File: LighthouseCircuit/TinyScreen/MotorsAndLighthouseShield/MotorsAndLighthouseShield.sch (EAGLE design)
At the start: 29 parts

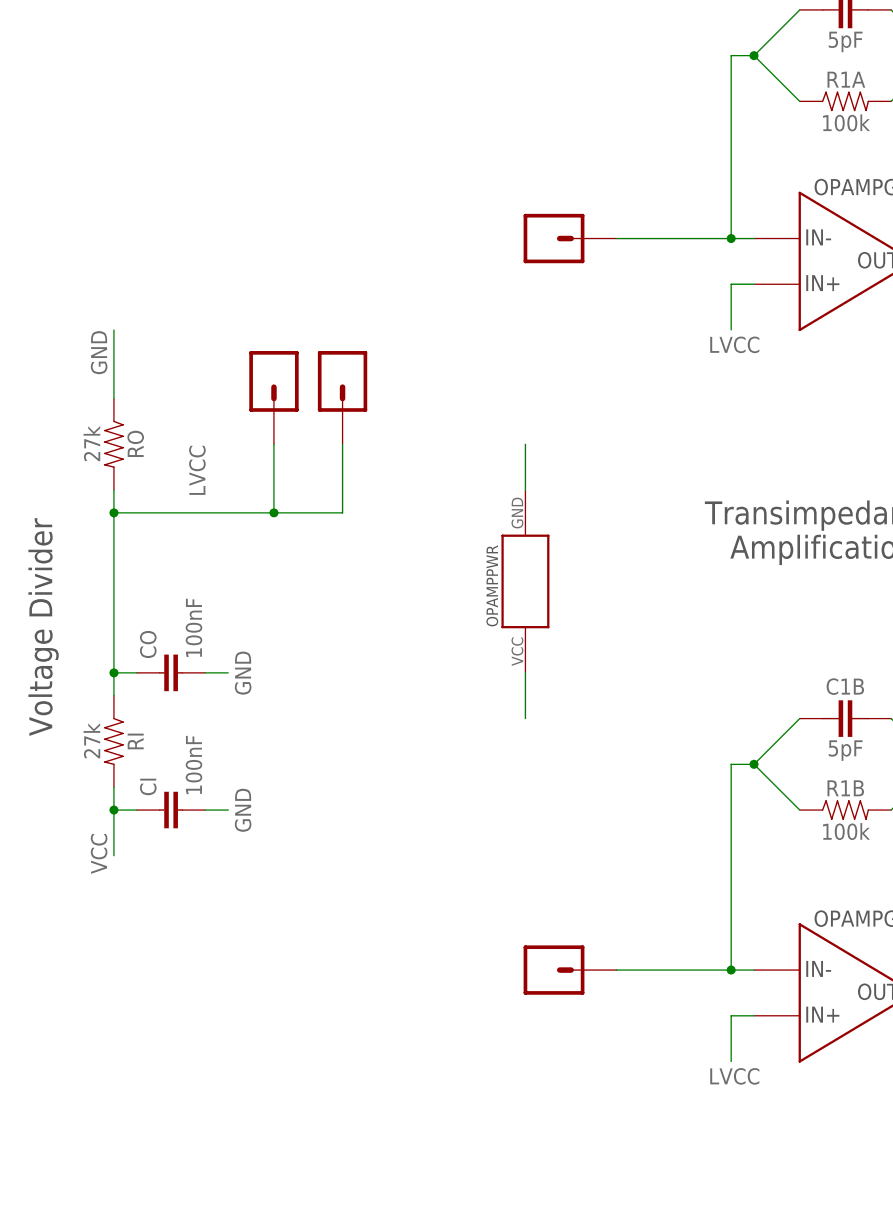
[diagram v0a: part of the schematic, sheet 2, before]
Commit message: Significantly stabilized the position calculation and the new driving model with independent PIDs for each wheel.
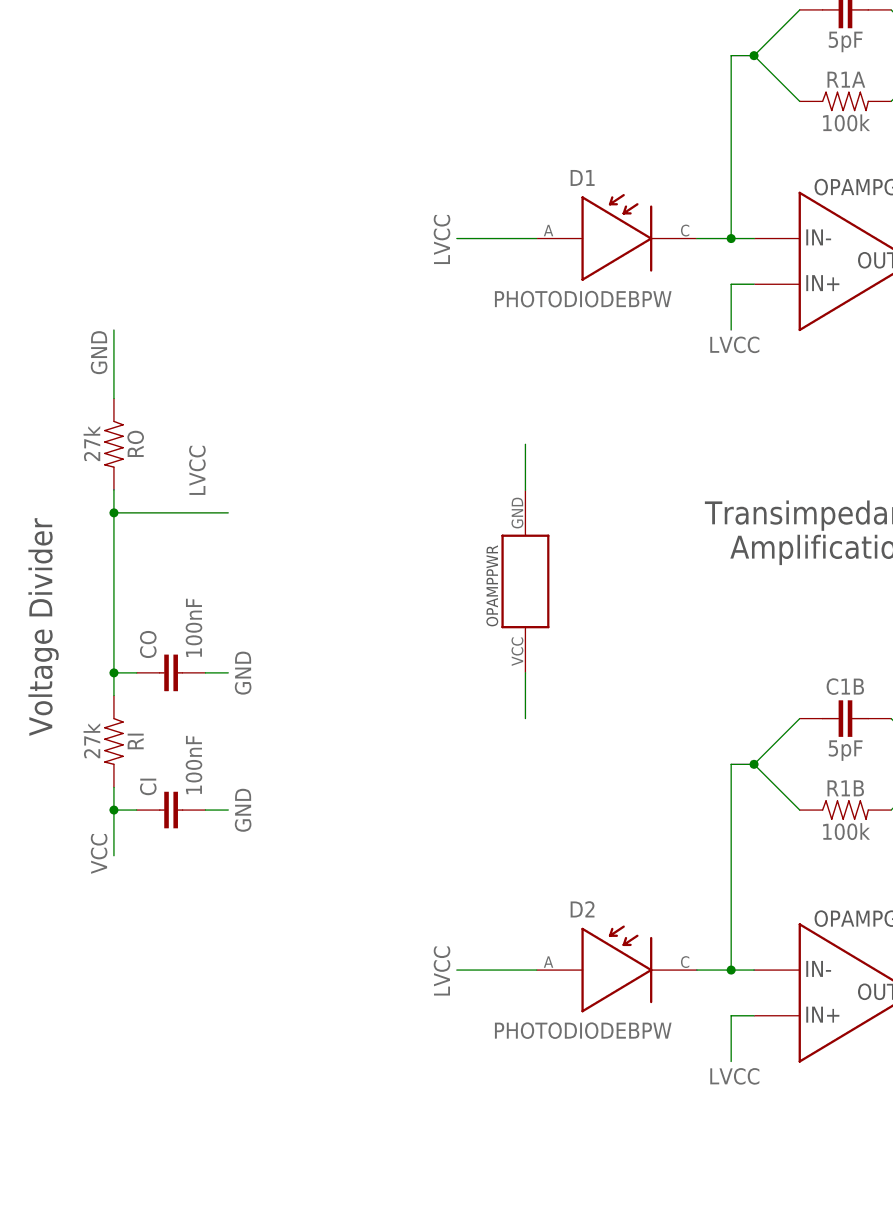
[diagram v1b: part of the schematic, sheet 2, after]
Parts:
- removed DIA, DIB, DOA, DOB: SINGLE-THROUGH-HOLE, ZippyComponentLibrary:SINGLE-THROUGH-HOLE
- added D1, D2: PHOTODIODEBPW, ZippyComponentLibrary:PHOTODIODEBPW
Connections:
- net D1IN1: now also D2.CATHODE; no longer DIB.1
- net D2IN1: now also D1.CATHODE; no longer DIA.1
- net IO6: now also MD.AIN1; no longer MD.BIN2
- net IO7: now also MD.AIN2; no longer MD.BIN1
- net IO8: now also MD.BIN1; no longer MD.AIN2
- net IO9: now also MD.BIN2; no longer MD.AIN1
- net LVCC: now also D1.ANODE, D2.ANODE; no longer DOA.1, DOB.1
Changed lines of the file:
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@@
 <part name="AO2" library="ZippyComponentLibrary" deviceset="SINGLE-THROUGH-HOLE" device=""/>
 <part name="HCM" library="ZippyComponentLibrary" deviceset="HIROSE-DF12-32DS" device="MALE" value="HIROSE-DF12-32DSMALE"/>
-<part name="DOA" library="ZippyComponentLibrary" deviceset="SINGLE-THROUGH-HOLE" device=""/>
-<part name="DIA" library="ZippyComponentLibrary" deviceset="SINGLE-THROUGH-HOLE" device=""/>
-<part name="DIB" library="ZippyComponentLibrary" deviceset="SINGLE-THROUGH-HOLE" device=""/>
-<part name="DOB" library="ZippyComponentLibrary" deviceset="SINGLE-THROUGH-HOLE" device=""/>
 <part name="VCO" library="ZippyComponentLibrary" deviceset="CAPACITOR" device="" value="0.1uF"/>
 <part name="VMO" library="ZippyComponentLibrary" deviceset="CAPACITOR" device="" value="0.1uF"/>
+<part name="D1" library="ZippyComponentLibrary" deviceset="PHOTODIODE" device="BPW"/>
+<part name="D2" library="ZippyComponentLibrary" deviceset="PHOTODIODE" device="BPW"/>
 </parts>
 <sheets>
@@
 </segment>
 <segment>
+<pinref part="MD" gate="A" pin="BIN2"/>
+<wire x1="208.28" y1="106.68" x2="200.66" y2="106.68" width="0.1524" layer="91"/>
+<label x="200.914" y="106.934" size="1.778" layer="95"/>
+</segment>
+</net>
+<net name="IO8" class="0">
+<segment>
+<pinref part="HCM" gate="G$1" pin="25"/>
+<wire x1="246.38" y1="25.4" x2="233.68" y2="25.4" width="0.1524" layer="91"/>
+<label x="233.426" y="25.654" size="1.778" layer="95"/>
+</segment>
+<segment>
+<pinref part="MD" gate="A" pin="BIN1"/>
+<wire x1="208.28" y1="109.22" x2="200.66" y2="109.22" width="0.1524" layer="91"/>
+<label x="200.914" y="109.474" size="1.778" layer="95"/>
+</segment>
+</net>
+<net name="IO3" class="0">
+<segment>
+<pinref part="HCM" gate="G$1" pin="30"/>
+<wire x1="269.24" y1="20.32" x2="279.4" y2="20.32" width="0.1524" layer="91"/>
+<label x="276.86" y="20.574" size="1.778" layer="95"/>
+</segment>
+</net>
+<net name="IO4" class="0">
+<segment>
+<pinref part="HCM" gate="G$1" pin="32"/>
+<wire x1="269.24" y1="17.78" x2="279.4" y2="17.78" width="0.1524" layer="91"/>
+<label x="276.86" y="18.034" size="1.778" layer="95"/>
+</segment>
+</net>
+<net name="IO6" class="0">
+<segment>
+<pinref part="HCM" gate="G$1" pin="29"/>
+<wire x1="246.38" y1="20.32" x2="233.68" y2="20.32" width="0.1524" layer="91"/>
+<label x="233.426" y="20.574" size="1.778" layer="95"/>
+</segment>
+<segment>
 <pinref part="MD" gate="A" pin="AIN1"/>
 <wire x1="208.28" y1="116.84" x2="200.66" y2="116.84" width="0.1524" layer="91"/>
@@
 </segment>
 </net>
-<net name="IO8" class="0">
-<segment>
-<pinref part="HCM" gate="G$1" pin="25"/>
-<wire x1="246.38" y1="25.4" x2="233.68" y2="25.4" width="0.1524" layer="91"/>
-<label x="233.426" y="25.654" size="1.778" layer="95"/>
+<net name="IO7" class="0">
+<segment>
+<pinref part="HCM" gate="G$1" pin="27"/>
+<wire x1="246.38" y1="22.86" x2="233.68" y2="22.86" width="0.1524" layer="91"/>
+<label x="233.426" y="23.114" size="1.778" layer="95"/>
 </segment>
 <segment>
@@
 <wire x1="208.28" y1="114.3" x2="200.66" y2="114.3" width="0.1524" layer="91"/>
 <label x="200.66" y="114.554" size="1.778" layer="95"/>
-</segment>
-</net>
-<net name="IO3" class="0">
-<segment>
-<pinref part="HCM" gate="G$1" pin="30"/>
-<wire x1="269.24" y1="20.32" x2="279.4" y2="20.32" width="0.1524" layer="91"/>
-<label x="276.86" y="20.574" size="1.778" layer="95"/>
-</segment>
-</net>
-<net name="IO4" class="0">
-<segment>
-<pinref part="HCM" gate="G$1" pin="32"/>
-<wire x1="269.24" y1="17.78" x2="279.4" y2="17.78" width="0.1524" layer="91"/>
-<label x="276.86" y="18.034" size="1.778" layer="95"/>
-</segment>
-</net>
-<net name="IO6" class="0">
-<segment>
-<pinref part="HCM" gate="G$1" pin="29"/>
-<wire x1="246.38" y1="20.32" x2="233.68" y2="20.32" width="0.1524" layer="91"/>
-<label x="233.426" y="20.574" size="1.778" layer="95"/>
-</segment>
-<segment>
-<pinref part="MD" gate="A" pin="BIN2"/>
-<wire x1="208.28" y1="106.68" x2="200.66" y2="106.68" width="0.1524" layer="91"/>
-<label x="200.914" y="106.934" size="1.778" layer="95"/>
-</segment>
-</net>
-<net name="IO7" class="0">
-<segment>
-<pinref part="HCM" gate="G$1" pin="27"/>
-<wire x1="246.38" y1="22.86" x2="233.68" y2="22.86" width="0.1524" layer="91"/>
-<label x="233.426" y="23.114" size="1.778" layer="95"/>
-</segment>
-<segment>
-<pinref part="MD" gate="A" pin="BIN1"/>
-<wire x1="208.28" y1="109.22" x2="200.66" y2="109.22" width="0.1524" layer="91"/>
-<label x="200.914" y="109.474" size="1.778" layer="95"/>
 </segment>
 </net>
@@
 <instance part="OPAMP" gate="G3" x="149.86" y="2.54"/>
 <instance part="OPAMP" gate="PWR" x="40.64" y="50.8" rot="R90"/>
-<instance part="DOA" gate="G$1" x="12.7" y="73.66" smashed="yes" rot="R270"/>
-<instance part="DIA" gate="G$1" x="43.18" y="88.9" smashed="yes"/>
-<instance part="DIB" gate="G$1" x="43.18" y="7.62" smashed="yes"/>
-<instance part="DOB" gate="G$1" x="20.32" y="73.66" smashed="yes" rot="R270"/>
+<instance part="D1" gate="G$1" x="50.8" y="88.9"/>
+<instance part="D2" gate="G$1" x="50.8" y="7.62"/>
 </instances>
 <busses>
@@
 <wire x1="-2.54" y1="40.64" x2="-5.08" y2="40.64" width="0.1524" layer="91"/>
 <junction x="-5.08" y="40.64"/>
-<pinref part="DOA" gate="G$1" pin="1"/>
-<wire x1="-5.08" y1="58.42" x2="12.7" y2="58.42" width="0.1524" layer="91"/>
-<wire x1="12.7" y1="58.42" x2="12.7" y2="66.04" width="0.1524" layer="91"/>
+<wire x1="-5.08" y1="58.42" x2="7.62" y2="58.42" width="0.1524" layer="91"/>
 <junction x="-5.08" y="58.42"/>
-<pinref part="DOB" gate="G$1" pin="1"/>
-<wire x1="12.7" y1="58.42" x2="20.32" y2="58.42" width="0.1524" layer="91"/>
-<wire x1="20.32" y1="58.42" x2="20.32" y2="66.04" width="0.1524" layer="91"/>
-<junction x="12.7" y="58.42"/>
 </segment>
 <segment>
@@
 <wire x1="137.16" y1="-27.94" x2="137.16" y2="-30.48" width="0.1524" layer="91"/>
 <label x="134.62" y="-33.02" size="1.778" layer="95"/>
+</segment>
+<segment>
+<label x="32.258" y="85.852" size="1.778" layer="95" rot="R90"/>
+<pinref part="D1" gate="G$1" pin="ANODE"/>
+<wire x1="41.91" y1="88.9" x2="33.02" y2="88.9" width="0.1524" layer="91"/>
+</segment>
+<segment>
+<label x="32.258" y="4.572" size="1.778" layer="95" rot="R90"/>
+<pinref part="D2" gate="G$1" pin="ANODE"/>
+<wire x1="41.91" y1="7.62" x2="33.02" y2="7.62" width="0.1524" layer="91"/>
 </segment>
 </net>
@@
 <net name="D2IN1" class="0">
 <segment>
-<wire x1="63.5" y1="88.9" x2="50.8" y2="88.9" width="0.1524" layer="91"/>
+<wire x1="63.5" y1="88.9" x2="59.69" y2="88.9" width="0.1524" layer="91"/>
 <pinref part="R1A" gate="G$1" pin="1"/>
 <wire x1="71.12" y1="104.14" x2="66.04" y2="109.22" width="0.1524" layer="91"/>
@@
 <junction x="63.5" y="88.9"/>
 <pinref part="OPAMP" gate="G1" pin="IN-"/>
-<pinref part="DIA" gate="G$1" pin="1"/>
+<pinref part="D1" gate="G$1" pin="CATHODE"/>
 </segment>
 </net>
@@
 <junction x="66.04" y="30.48"/>
 <pinref part="OPAMP" gate="G4" pin="IN-"/>
-<pinref part="DIB" gate="G$1" pin="1"/>
-<wire x1="63.5" y1="7.62" x2="50.8" y2="7.62" width="0.1524" layer="91"/>
+<wire x1="63.5" y1="7.62" x2="59.69" y2="7.62" width="0.1524" layer="91"/>
 <junction x="63.5" y="7.62"/>
-</segment>
-</net>
+<pinref part="D2" gate="G$1" pin="CATHODE"/>
+</segment>
+</net>
